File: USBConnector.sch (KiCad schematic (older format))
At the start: 11 parts, among them J3 USB4085-GF-A

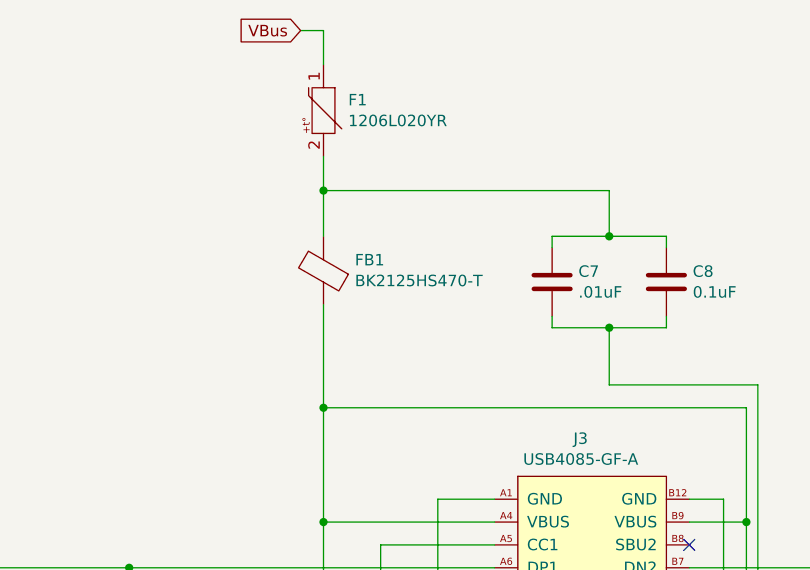
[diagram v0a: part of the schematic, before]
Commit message: Initial layout complete. Pins moved to make layout easy
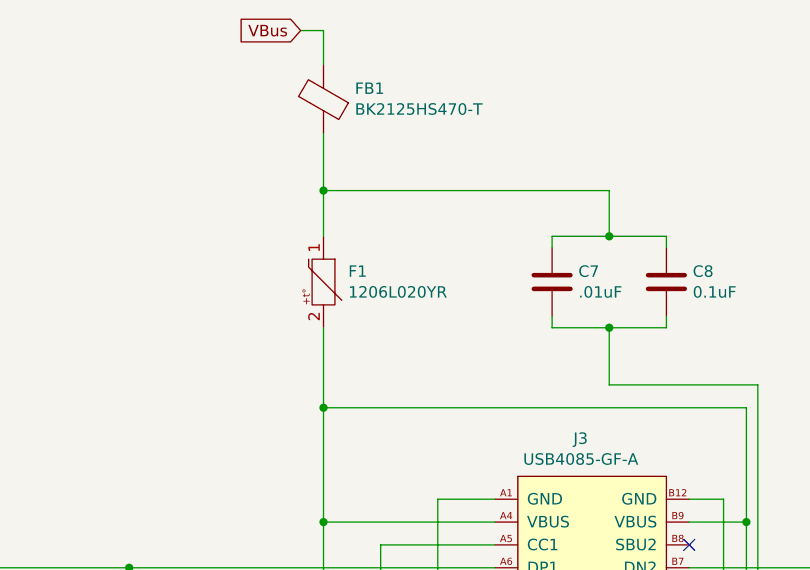
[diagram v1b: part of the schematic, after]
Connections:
- net VBus: now also FB1.2; no longer F1.1
- net at D5.1, J3.A4 (VBUS), J3.A9 (VBUS)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: now also F1.2; no longer FB1.1
- net at C7.1, C8.1: now also F1.1, FB1.1; no longer F1.2, FB1.2
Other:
- moved on the sheet: F1, FB1
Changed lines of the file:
@@
 L Zack_Inductors:BK2125HS470-T FB1
 U 1 1 5F446B75
-P 4600 2350
-F 0 "FB1" V 4646 2213 50  0000 R CNN
-F 1 "BK2125HS470-T" V 4555 2213 50  0000 R CNN
-F 2 "Inductor_SMD:L_0805_2012Metric" H 4600 2280 50  0001 C CNN
-F 3 "~" V 4600 2350 50  0001 C CNN
-F 4 "Taiyo Yuden" H 4600 2350 50  0001 C CNN "Manufacturer 1 Name"
-F 5 "BK2125HS470-T" H 4600 2350 50  0001 C CNN "Manufacturer 1 Part Number"
-	1    4600 2350
+P 4600 1600
+F 0 "FB1" V 4646 1463 50  0000 R CNN
+F 1 "BK2125HS470-T" V 4555 1463 50  0000 R CNN
+F 2 "Inductor_SMD:L_0805_2012Metric" H 4600 1530 50  0001 C CNN
+F 3 "~" V 4600 1600 50  0001 C CNN
+F 4 "Taiyo Yuden" H 4600 1600 50  0001 C CNN "Manufacturer 1 Name"
+F 5 "BK2125HS470-T" H 4600 1600 50  0001 C CNN "Manufacturer 1 Part Number"
+	1    4600 1600
 	0    -1   -1   0
 $EndComp
@@
 Connection ~ 4600 2950
 Wire Wire Line
-	4600 2950 4600 2500
+	4600 2950 4600 2600
 Wire Wire Line
 	5350 3950 4600 3950
@@
 L Zack_Resistors:1206L020YR F1
 U 1 1 5F476EE6
-P 4600 1650
-F 0 "F1" V 4554 1758 50  0000 L CNN
-F 1 "1206L020YR" V 4645 1758 50  0000 L CNN
-F 2 "Fuse:Fuse_1206_3216Metric" H 4600 1750 50  0001 C CNN
-F 3 "" H 4600 1750 50  0001 C CNN
-F 4 "Littelfuse Inc." H 4600 1650 50  0001 C CNN "Manufacturer 1 Name"
-F 5 "1206L020YR" H 4600 1650 50  0001 C CNN "Manufacturer 1 Part Number"
-	1    4600 1650
+P 4600 2400
+F 0 "F1" V 4554 2508 50  0000 L CNN
+F 1 "1206L020YR" V 4645 2508 50  0000 L CNN
+F 2 "Fuse:Fuse_1206_3216Metric" H 4600 2500 50  0001 C CNN
+F 3 "" H 4600 2500 50  0001 C CNN
+F 4 "Littelfuse Inc." H 4600 2400 50  0001 C CNN "Manufacturer 1 Name"
+F 5 "1206L020YR" H 4600 2400 50  0001 C CNN "Manufacturer 1 Part Number"
+	1    4600 2400
 	0    1    1    0
 $EndComp
 Wire Wire Line
-	4600 1850 4600 2000
+	4600 1750 4600 2000
 Wire Wire Line
 	4500 1300 4600 1300

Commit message: Silkscreen REFDES resized and aligned
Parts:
- F1: footprint Fuse:Fuse_1206_3216Metric -> Zack_Fuses:Fuse_1206_3216Metric
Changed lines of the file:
@@
 F 0 "F1" V 4554 2508 50  0000 L CNN
 F 1 "1206L020YR" V 4645 2508 50  0000 L CNN
-F 2 "Fuse:Fuse_1206_3216Metric" H 4600 2500 50  0001 C CNN
+F 2 "Zack_Fuses:Fuse_1206_3216Metric" H 4600 2500 50  0001 C CNN
 F 3 "" H 4600 2500 50  0001 C CNN
 F 4 "Littelfuse Inc." H 4600 2400 50  0001 C CNN "Manufacturer 1 Name"
